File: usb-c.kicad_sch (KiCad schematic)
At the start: 12 parts, among them J1 USB_C_Receptacle_USB2.0_16P, U3 USBLC6-2SC6, U4 CP2102N-Axx-xQFN20

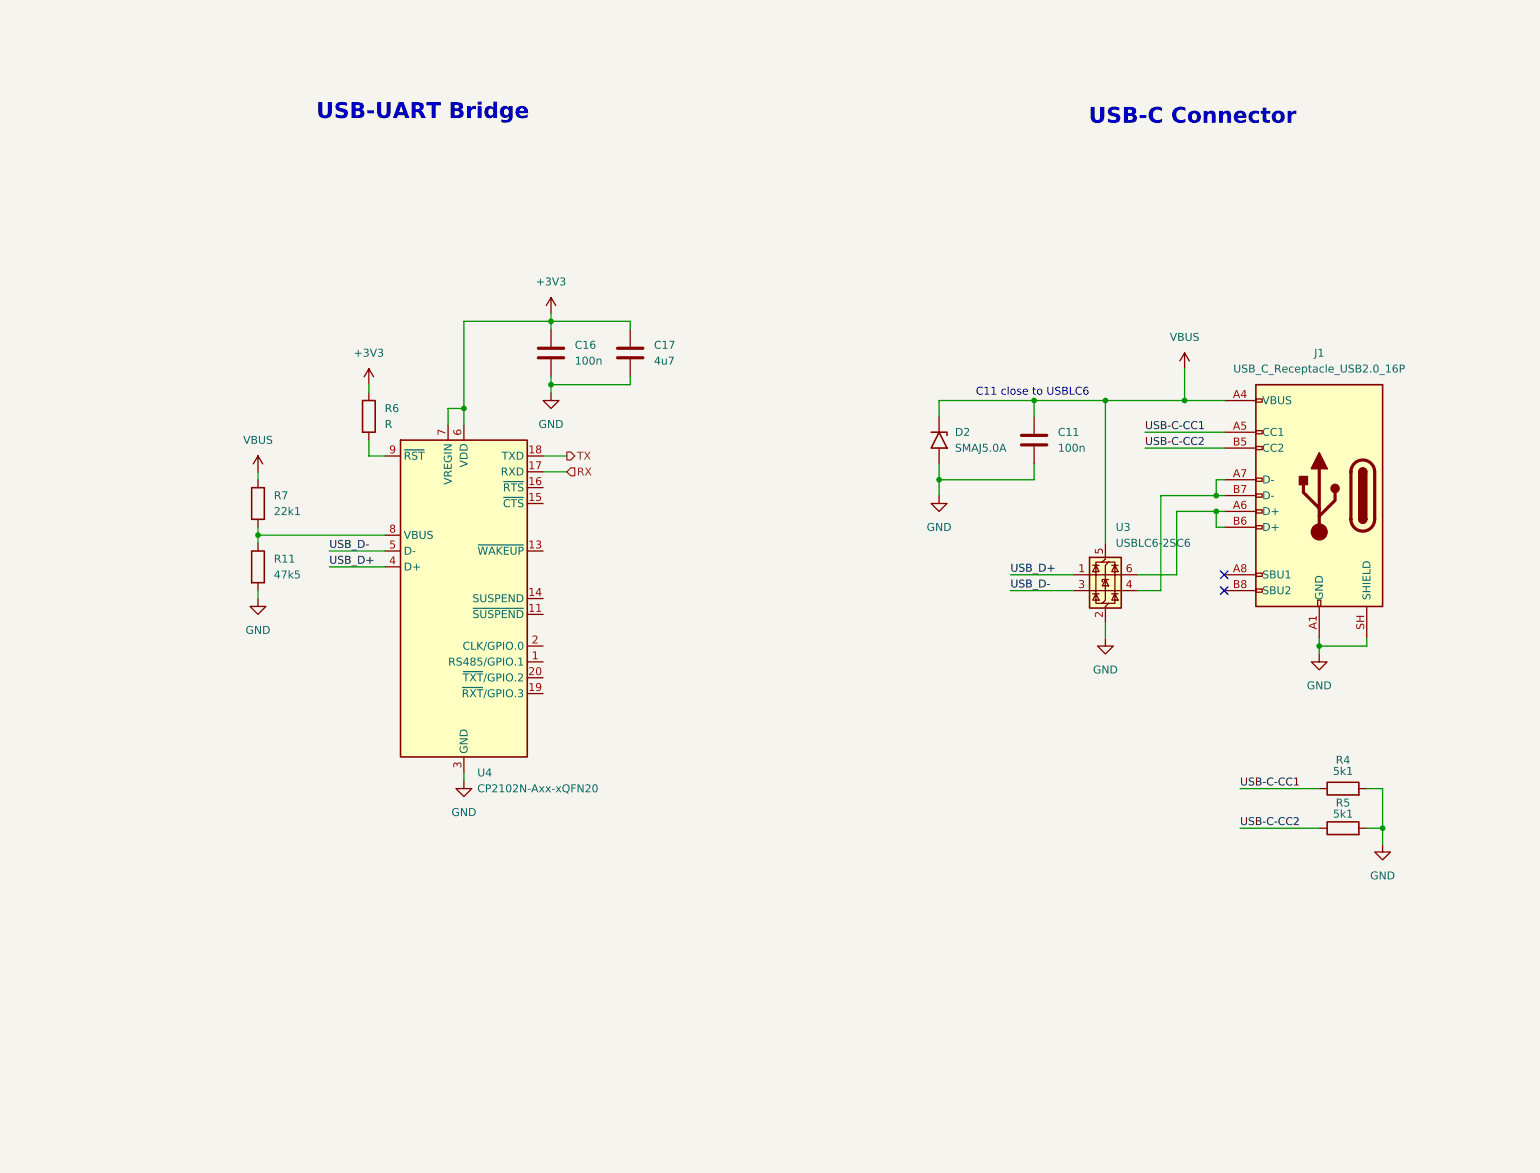
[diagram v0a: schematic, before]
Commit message: Add servo connectors
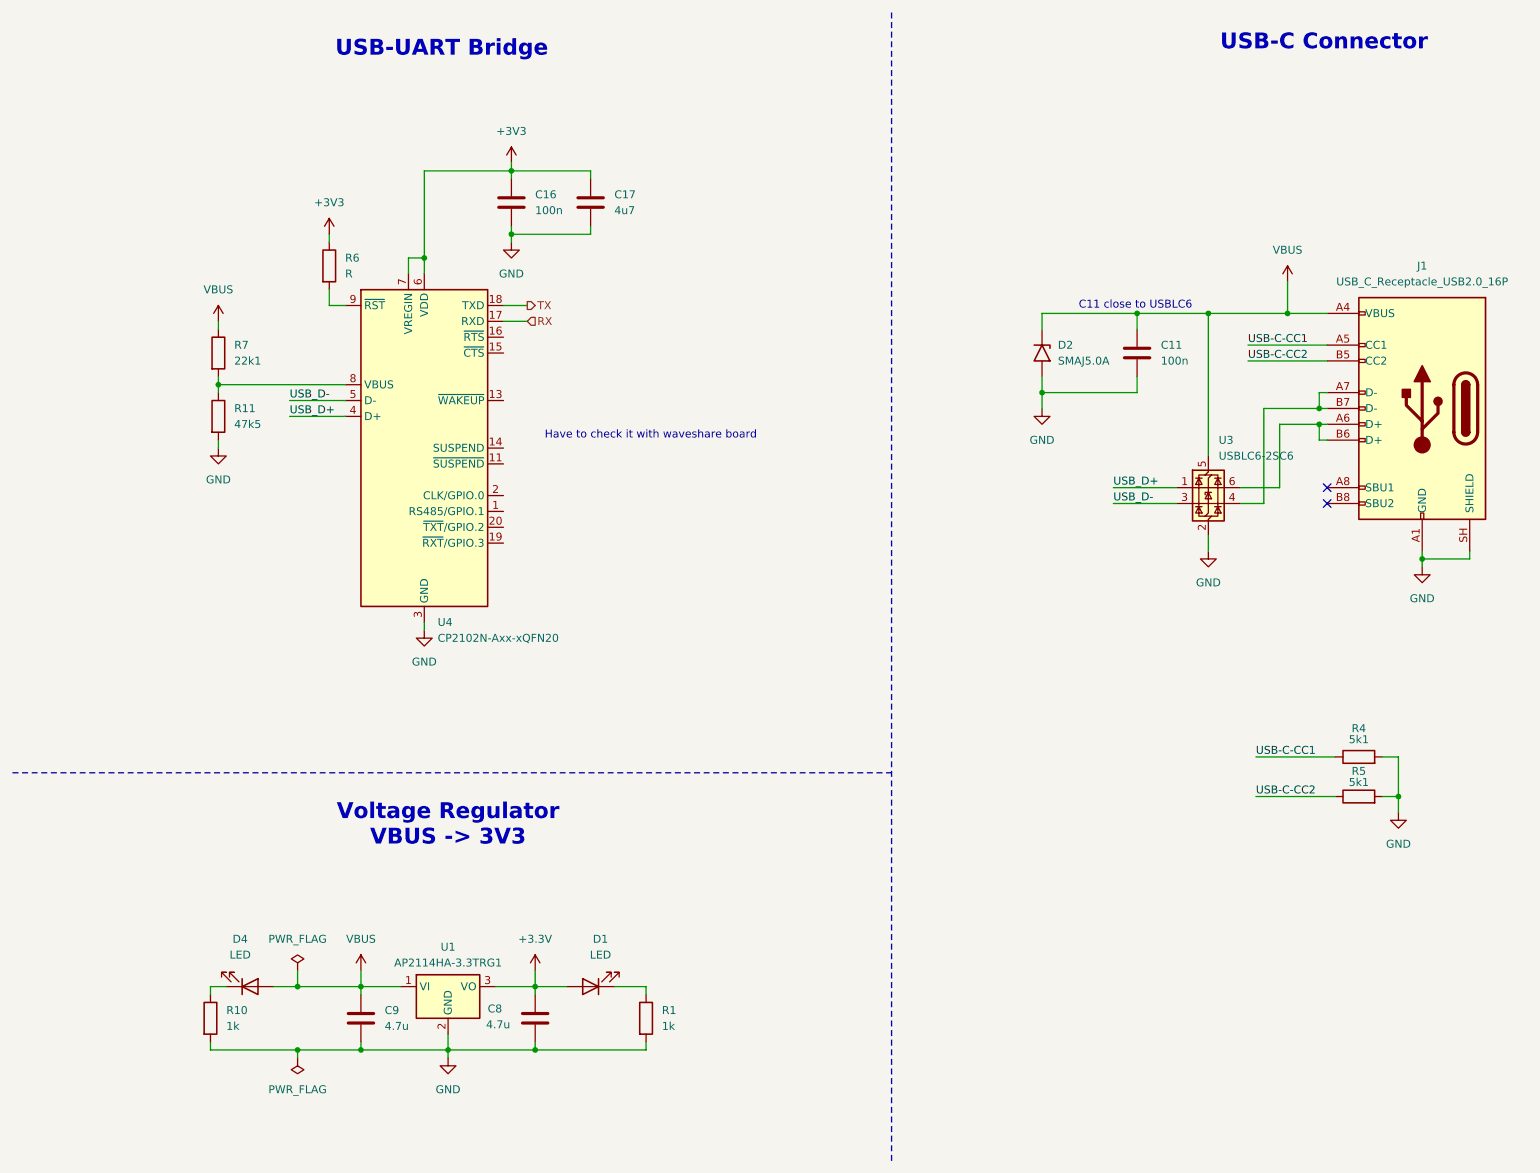
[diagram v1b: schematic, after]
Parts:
- added C8, C9: 4.7u, Capacitor_SMD:C_0805_2012Metric_Pad1.18x1.45mm_HandSolder, symbol Device:C
- added D1, D4: LED, LED_SMD:LED_0805_2012Metric_Pad1.15x1.40mm_HandSolder, symbol Device:LED
- added R1, R10: 1k, Resistor_SMD:R_0402_1005Metric_Pad0.72x0.64mm_HandSolder, symbol Device:R
- added U1: AP2114HA-3.3TRG1, Package_TO_SOT_SMD:SOT-223-3_TabPin2, symbol mc_custom_symbols:AP2114H-3.3TRG1
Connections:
- net GND: now also C8.2, C9.2, R1.2, R10.2, U1.2 (GND)
- net VBUS: now also C9.1, D4.2 (A), U1.1 (VI)
- new net: D4.1 (K), R10.1
- new net: D1.1 (K), R1.1
- new net +3.3V: C8.1, D1.2 (A), U1.3 (VO)
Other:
- note added: "Have to check it with waveshare board"
- note added: "Voltage Regulator VBUS -> 3V3"
- moved on the sheet: C11, C16, C17, D2, J1, R11, R4, R5, R6, R7, U3, U4
